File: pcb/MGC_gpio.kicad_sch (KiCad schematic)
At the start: 47 parts, among them J11 103R012BB100, J12 103R012BB100, J13 103R012BB100, J14 Conn_02x10_Odd_Even, J15 Conn_02x10_Odd_Even, J16 Conn_01x03, J17 Conn_01x01_Pin, J18 Conn_01x02_Pin, J19 Conn_01x02_Pin, J20 Conn_01x02_Pin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

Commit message: Adapt device values
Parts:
- D0, D1, D2, D3, D4, D5: value LED -> Green
- D6: value LED -> Yellow
- D7: value LED -> Red
- R1, R2, R3, R4, R5, R6: value 560 -> 270
- R7, R8: value 560 -> 330
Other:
- moved on the sheet: R25, R26, R27, R28, SW0, SW1, SW2, SW3

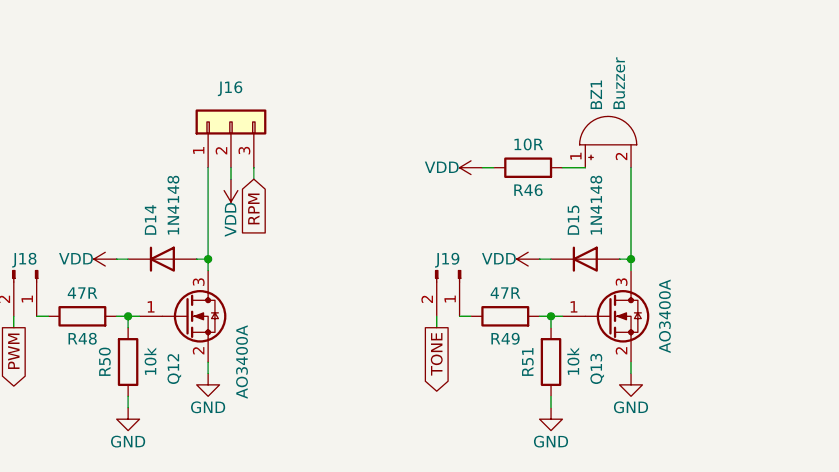
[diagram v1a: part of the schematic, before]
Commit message: Add missing vendor(id)
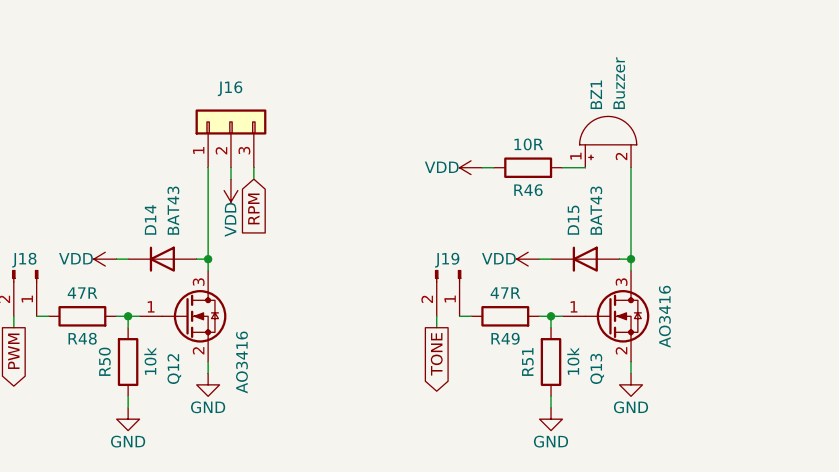
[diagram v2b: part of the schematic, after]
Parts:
- BZ1: HTL (none) -> 102851
- D0, D1, D2, D3, D4, D5: HTL (none) -> 100459
- D14, D15: value 1N4148 -> BAT43; HTL (none) -> 100206
- D6: HTL (none) -> 100457
- D7: HTL (none) -> 100458
- J14, J15: HTL (none) -> 101548
- J16: DigiKey (none) -> WM4201-ND
- J17: HTL (none) -> 101521
- J18, J19, J20: DigiKey (none) -> HDR100IMP40M-G-V-SM-ND
- Q12, Q13: value AO3400A -> AO3416; HTL (none) -> 103512
- R1, R2, R3, R4, R5, R6: HTL (none) -> 102938
- R25, R26, R27, R28, R47: HTL (none) -> 102959
- R46: HTL (none) -> 102913
- R48, R49: HTL (none) -> 102927
- R50, R51: HTL (none) -> 102967
- R7, R8: HTL (none) -> 102940
- RV1: HTL (none) -> 102614
- SW0, SW1, SW2, SW3: HTL (none) -> 101613

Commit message: Fix connector pin direction
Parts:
- J18, J19, J20: footprint Connector_PinHeader_2.54mm:PinHeader_1x02_P2.54mm_Vertical_SMD_Pin1Left -> Connector_PinHeader_2.54mm:PinHeader_1x02_P2.54mm_Vertical_SMD_Pin1Right
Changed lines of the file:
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@@
 			)
 		)
-		(property "Footprint" "Connector_PinHeader_2.54mm:PinHeader_1x02_P2.54mm_Vertical_SMD_Pin1Left"
+		(property "Footprint" "Connector_PinHeader_2.54mm:PinHeader_1x02_P2.54mm_Vertical_SMD_Pin1Right"
 			(at 125.73 166.37 0)
 			(effects
@@
 			)
 		)
-		(property "Footprint" "Connector_PinHeader_2.54mm:PinHeader_1x02_P2.54mm_Vertical_SMD_Pin1Left"
+		(property "Footprint" "Connector_PinHeader_2.54mm:PinHeader_1x02_P2.54mm_Vertical_SMD_Pin1Right"
 			(at 78.74 166.37 0)
 			(effects
@@
 			)
 		)
-		(property "Footprint" "Connector_PinHeader_2.54mm:PinHeader_1x02_P2.54mm_Vertical_SMD_Pin1Left"
+		(property "Footprint" "Connector_PinHeader_2.54mm:PinHeader_1x02_P2.54mm_Vertical_SMD_Pin1Right"
 			(at 52.07 167.64 0)
 			(effects
